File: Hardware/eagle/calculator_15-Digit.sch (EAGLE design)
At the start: 145 parts, among them M1 IRLML6402, M10 IRLML6402, M11 IRLML6402, M12 IRLML6402, M2 IRLML6402, M3 IRLML6402, M4 IRLML6402, M5 IRLML6402, M6 IRLML6402, M7 IRLML6402, M8 IRLML6402, M9 IRLML6402, U1 74HC4051_MUX, U2 TC1262-3.3VDB, U3 ATMEGA1284P-PU, U5 CON, X1 MICROMATCH-12, X3 MICROMATCH-12, Y2 12MHz

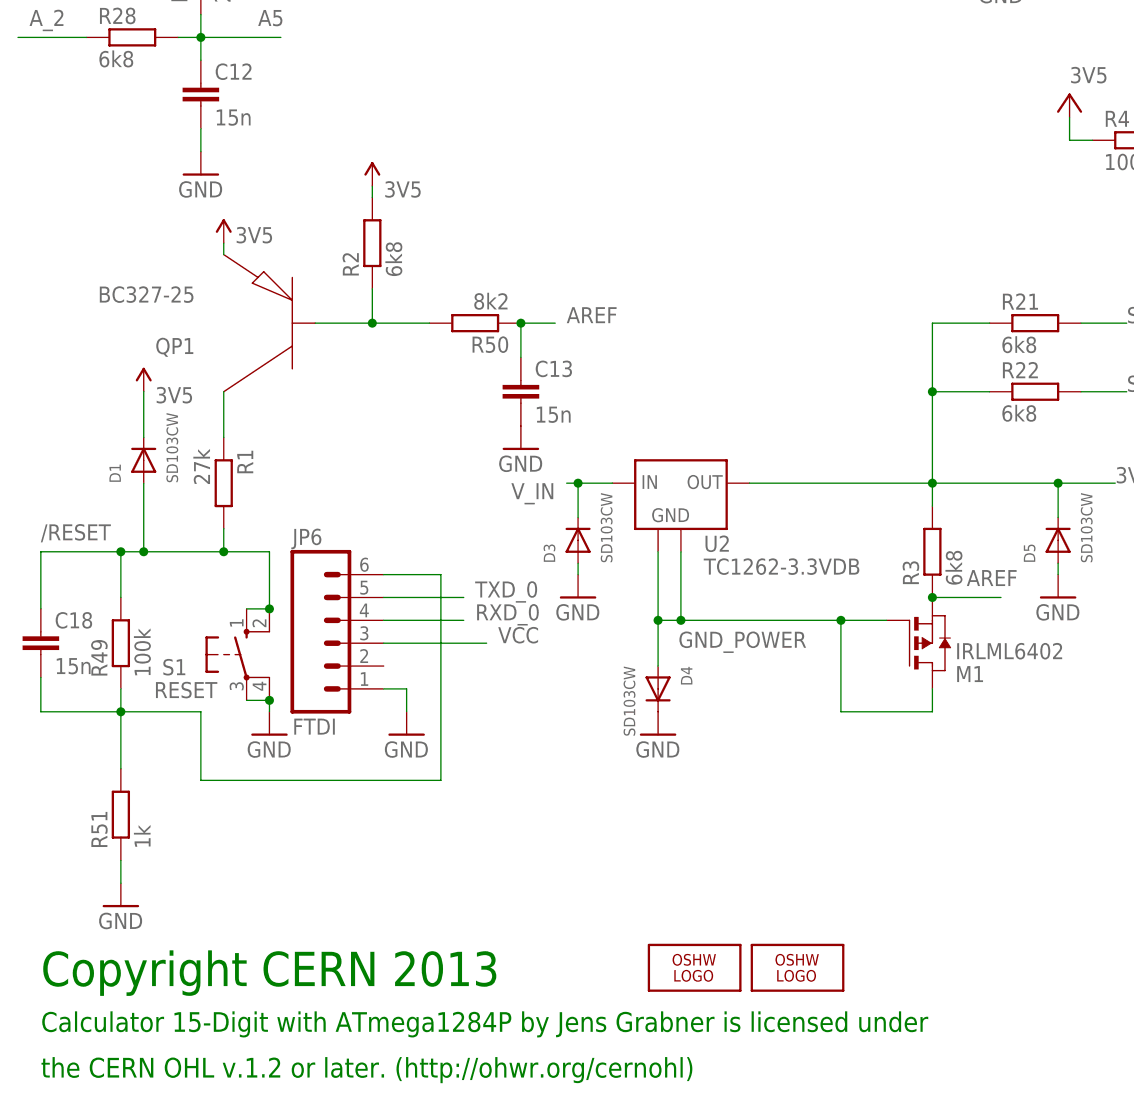
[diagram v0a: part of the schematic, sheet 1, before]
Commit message: new Switch Layout - with Kipptaster
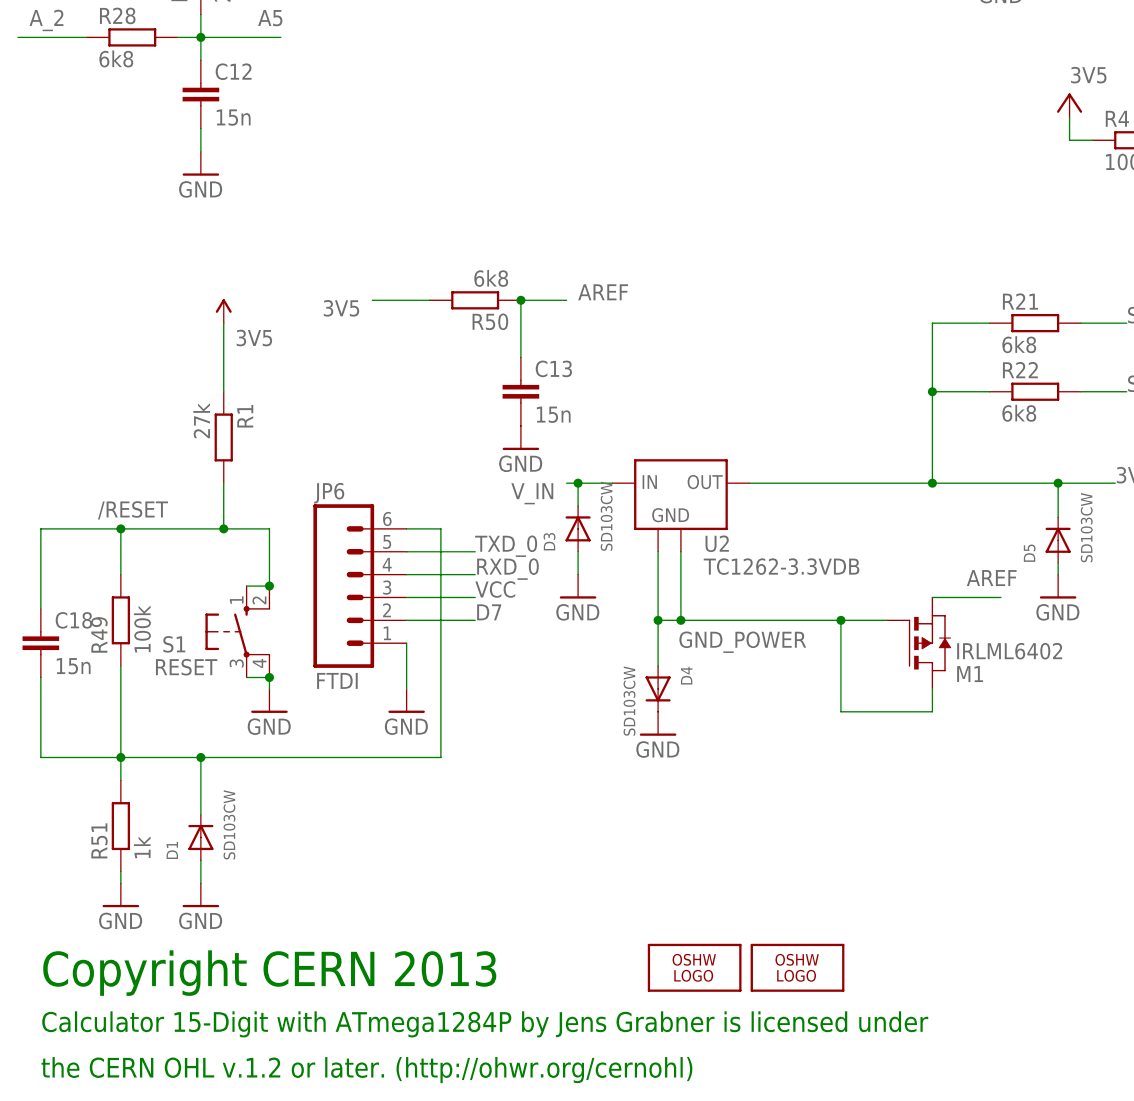
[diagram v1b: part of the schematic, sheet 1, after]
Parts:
- removed QP1: BC327-25, sym:PNP
- removed R2, R3: 6k8, rcl:R-EU_0204/7
- added JP13, JP14: PINHD-2X7, pinhead:PINHD-2X7
- R50: value 8k2 -> 6k8
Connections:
- removed net N$10: QP1.C, R1.1
- removed net N$13: QP1.B, R2.1, R50.2
- net /RESET: no longer D1.A
- net 3V5: now also R1.1; no longer D1.C, QP1.E, R2.2, R3.2
- net AREF: no longer R3.1
- net CA_PWM: now also JP13.1, JP13.2, JP14.13, JP14.14, JP14.8
- net D10: now also JP13.9
- net D11: now also JP13.10
- net D12: now also JP14.1
- net D13: now also JP14.2
- net D19: now also JP14.7
- net D20: now also JP14.6
- net D21: now also JP14.5
- net D22: now also JP14.4
- net D23: now also JP14.3
- net D5: now also JP13.8
- net D6: now also JP13.7
- net D7: now also JP6.2
- net GND: now also D1.A
- net IO_A: now also JP13.6
- net IO_A__: now also JP13.11
- net IO_B: now also JP13.5
- net IO_B__: now also JP13.12
- net IO_C: now also JP13.4
- net IO_C__: now also JP13.13
- net IO_D: now also JP13.3
- net IO_DP: now also JP14.9
- net IO_D__: now also JP13.14
- net IO_E: now also JP14.12
- net IO_F: now also JP14.11
- net IO_G: now also JP14.10
- net N$12: now also D1.C
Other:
- moved on the sheet: D1, D3, JP6, R1, R49, R50, R51, S1

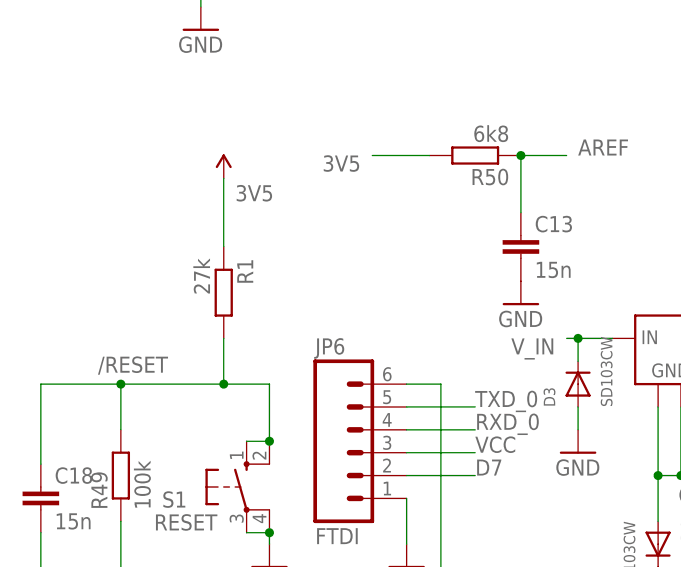
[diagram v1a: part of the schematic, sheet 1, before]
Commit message: MR(); MS(); M+=(); Display Status
Display whe to or more switch pressed.
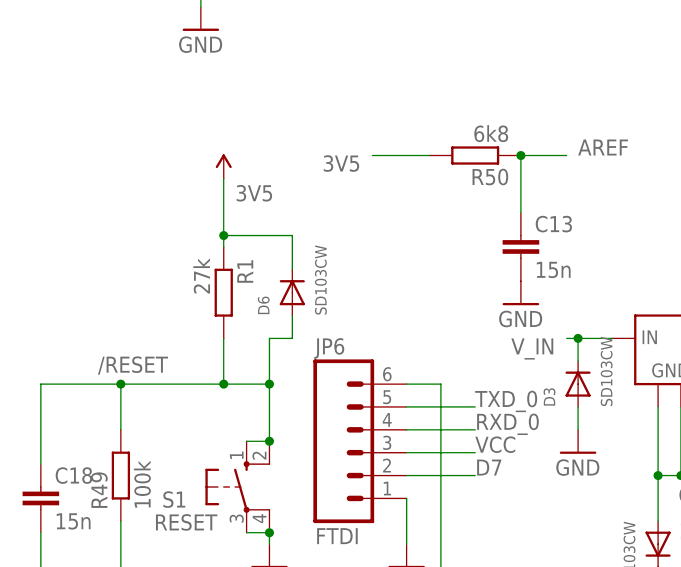
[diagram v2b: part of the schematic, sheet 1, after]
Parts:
- added D6: SD103CW, BaseApp:DIODESMA
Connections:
- net /RESET: now also D6.A
- net 3V5: now also D6.C
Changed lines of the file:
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@@
 <setting verticaltext="up"/>
 </settings>
-<grid distance="50" unitdist="mil" unit="mil" style="lines" multiple="1" display="no" altdistance="0.05" altunitdist="inch" altunit="inch"/>
+<grid distance="0.05" unitdist="inch" unit="inch" style="lines" multiple="1" display="no" altdistance="0.05" altunitdist="inch" altunit="inch"/>
 <layers>
 <layer number="1" name="Top" color="4" fill="1" visible="no" active="no"/>
@@
 <part name="D1" library="BaseApp" deviceset="DIODE" device="SMA" value="SD103CW"/>
 <part name="GND7" library="SparkFun" deviceset="GND" device=""/>
+<part name="D6" library="BaseApp" deviceset="DIODE" device="SMA" value="SD103CW"/>
 </parts>
 <sheets>
@@
 <attribute name="VALUE" x="20.32" y="21.59" size="1.778" layer="96"/>
 </instance>
+<instance part="D6" gate="G$1" x="33.02" y="76.2" rot="R90"/>
 </instances>
 <busses>
@@
 <pinref part="R1" gate="G$1" pin="2"/>
 <pinref part="R49" gate="G$1" pin="2"/>
+<wire x1="30.48" y1="66.04" x2="30.48" y2="71.12" width="0.1524" layer="91"/>
+<junction x="30.48" y="66.04"/>
+<wire x1="30.48" y1="71.12" x2="33.02" y2="71.12" width="0.1524" layer="91"/>
+<pinref part="D6" gate="G$1" pin="A"/>
+<wire x1="33.02" y1="71.12" x2="33.02" y2="73.66" width="0.1524" layer="91"/>
 </segment>
 <segment>
@@
 <pinref part="P+5" gate="1" pin="VCC"/>
 <label x="26.67" y="86.36" size="1.778" layer="95"/>
-<wire x1="25.4" y1="81.28" x2="25.4" y2="88.9" width="0.1524" layer="91"/>
+<wire x1="25.4" y1="81.28" x2="25.4" y2="82.55" width="0.1524" layer="91"/>
 <pinref part="R1" gate="G$1" pin="1"/>
-</segment>
-<segment>
+<pinref part="D6" gate="G$1" pin="C"/>
+<wire x1="25.4" y1="82.55" x2="25.4" y2="88.9" width="0.1524" layer="91"/>
+<wire x1="33.02" y1="78.74" x2="33.02" y2="82.55" width="0.1524" layer="91"/>
+<wire x1="33.02" y1="82.55" x2="25.4" y2="82.55" width="0.1524" layer="91"/>
+<junction x="25.4" y="82.55"/>
+</segment>
+<segment>

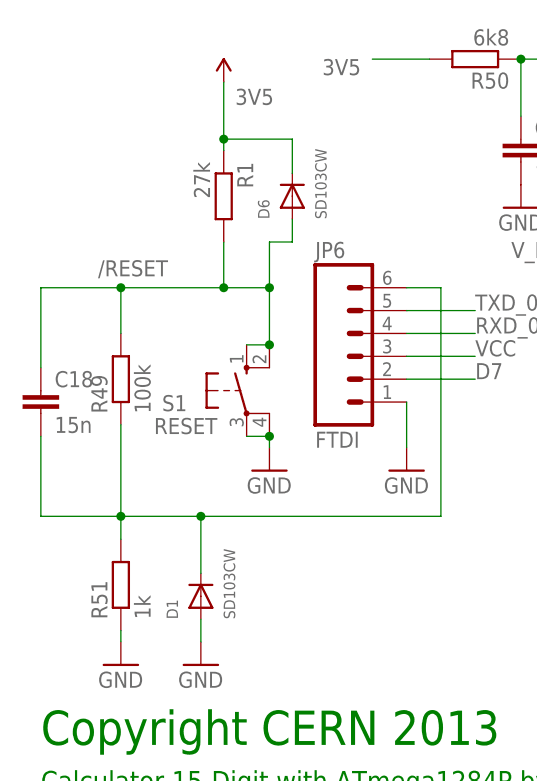
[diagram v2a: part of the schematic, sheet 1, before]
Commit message: RingBufCPP added
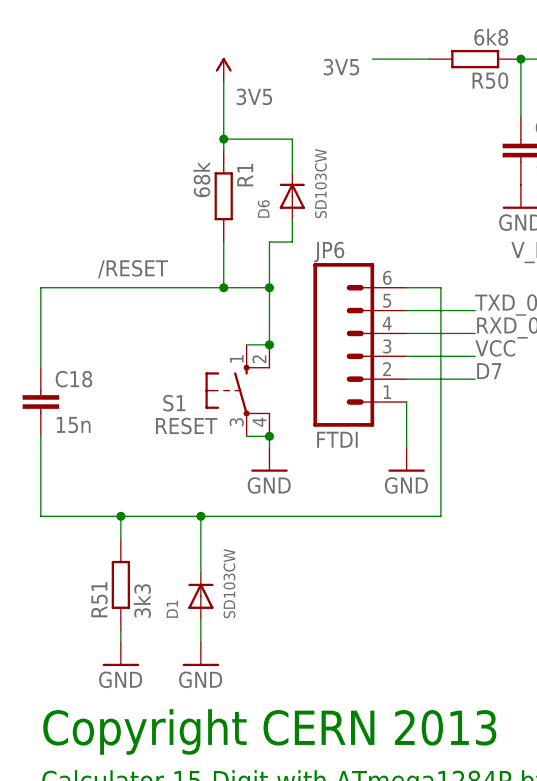
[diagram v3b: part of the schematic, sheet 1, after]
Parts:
- removed R49: 100k, rcl:R-EU_0204/7
- M10, M11, M3, M4, M5, M6, M7, M8, M9: value IRLML6402 -> IRLML6401
- R1: value 27k -> 68k
- R51: value 1k -> 3k3
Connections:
- net /RESET: no longer R49.2
- net N$12: no longer R49.1
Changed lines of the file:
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@@
 <setting verticaltext="up"/>
 </settings>
-<grid distance="0.05" unitdist="inch" unit="inch" style="lines" multiple="1" display="no" altdistance="0.05" altunitdist="inch" altunit="inch"/>
+<grid distance="0.1" unitdist="inch" unit="inch" style="lines" multiple="1" display="no" altdistance="0.05" altunitdist="inch" altunit="inch"/>
 <layers>
 <layer number="1" name="Top" color="4" fill="1" visible="no" active="no"/>
@@
 <part name="GND20" library="SparkFun" deviceset="GND" device=""/>
 <part name="GND21" library="SparkFun" deviceset="GND" device=""/>
-<part name="M3" library="IRLML6402" deviceset="IRLML6402" device=""/>
-<part name="M4" library="IRLML6402" deviceset="IRLML6402" device=""/>
-<part name="M5" library="IRLML6402" deviceset="IRLML6402" device=""/>
-<part name="M6" library="IRLML6402" deviceset="IRLML6402" device=""/>
-<part name="M7" library="IRLML6402" deviceset="IRLML6402" device=""/>
-<part name="M8" library="IRLML6402" deviceset="IRLML6402" device=""/>
-<part name="M9" library="IRLML6402" deviceset="IRLML6402" device=""/>
-<part name="M10" library="IRLML6402" deviceset="IRLML6402" device=""/>
-<part name="M11" library="IRLML6402" deviceset="IRLML6402" device=""/>
+<part name="M3" library="IRLML6402" deviceset="IRLML6402" device="" value="IRLML6401"/>
+<part name="M4" library="IRLML6402" deviceset="IRLML6402" device="" value="IRLML6401"/>
+<part name="M5" library="IRLML6402" deviceset="IRLML6402" device="" value="IRLML6401"/>
+<part name="M6" library="IRLML6402" deviceset="IRLML6402" device="" value="IRLML6401"/>
+<part name="M7" library="IRLML6402" deviceset="IRLML6402" device="" value="IRLML6401"/>
+<part name="M8" library="IRLML6402" deviceset="IRLML6402" device="" value="IRLML6401"/>
+<part name="M9" library="IRLML6402" deviceset="IRLML6402" device="" value="IRLML6401"/>
+<part name="M10" library="IRLML6402" deviceset="IRLML6402" device="" value="IRLML6401"/>
+<part name="M11" library="IRLML6402" deviceset="IRLML6402" device="" value="IRLML6401"/>
 <part name="FRAME3" library="frames" deviceset="LETTER_L" device="" value="frame"/>
 <part name="D29" library="BaseApp" deviceset="DIODE" device="SMA" value="SD103CW"/>
@@
 <part name="U3" library="Atmel_By_element14_Batch_1-00" deviceset="ATMEGA1284P-PU" device=""/>
 <part name="R50" library="rcl" deviceset="R-EU_" device="0204/7" value="6k8"/>
-<part name="R1" library="rcl" deviceset="R-EU_" device="0204/7" value="27k"/>
+<part name="R1" library="rcl" deviceset="R-EU_" device="0204/7" value="68k"/>
 <part name="R4" library="rcl" deviceset="R-EU_" device="0204/7" value="100"/>
-<part name="R49" library="rcl" deviceset="R-EU_" device="0204/7" value="100k"/>
-<part name="R51" library="rcl" deviceset="R-EU_" device="0204/7" value="1k"/>
+<part name="R51" library="rcl" deviceset="R-EU_" device="0204/7" value="3k3"/>
 <part name="R34" library="rcl" deviceset="R-EU_" device="0204/7" value="6k8"/>
 <part name="R48" library="rcl" deviceset="R-EU_" device="0204/7" value="1k"/>
@@
 <instance part="R1" gate="G$1" x="25.4" y="76.2" rot="R270"/>
 <instance part="R4" gate="G$1" x="127" y="109.22"/>
-<instance part="R49" gate="G$1" x="13.97" y="55.88" rot="R90"/>
 <instance part="R51" gate="G$1" x="13.97" y="33.02" rot="R90"/>
 <instance part="JP1" gate="G$1" x="238.76" y="113.03"/>
@@
 <segment>
 <wire x1="30.48" y1="66.04" x2="25.4" y2="66.04" width="0.1524" layer="91"/>
-<wire x1="25.4" y1="66.04" x2="13.97" y2="66.04" width="0.1524" layer="91"/>
-<wire x1="13.97" y1="66.04" x2="5.08" y2="66.04" width="0.1524" layer="91"/>
+<wire x1="25.4" y1="66.04" x2="5.08" y2="66.04" width="0.1524" layer="91"/>
 <wire x1="30.48" y1="66.04" x2="30.48" y2="59.69" width="0.1524" layer="91"/>
 <label x="11.43" y="67.31" size="1.778" layer="95"/>
@@
 <wire x1="25.4" y1="71.12" x2="25.4" y2="66.04" width="0.1524" layer="91"/>
 <junction x="25.4" y="66.04"/>
-<wire x1="13.97" y1="60.96" x2="13.97" y2="66.04" width="0.1524" layer="91"/>
-<junction x="13.97" y="66.04"/>
 <pinref part="C18" gate="G$1" pin="1"/>
 <pinref part="R1" gate="G$1" pin="2"/>
-<pinref part="R49" gate="G$1" pin="2"/>
 <wire x1="30.48" y1="66.04" x2="30.48" y2="71.12" width="0.1524" layer="91"/>
 <junction x="30.48" y="66.04"/>
@@
 <wire x1="13.97" y1="38.1" x2="13.97" y2="40.64" width="0.1524" layer="91"/>
 <pinref part="C18" gate="G$1" pin="2"/>
-<wire x1="13.97" y1="40.64" x2="13.97" y2="50.8" width="0.1524" layer="91"/>
 <wire x1="5.08" y1="49.53" x2="5.08" y2="40.64" width="0.1524" layer="91"/>
 <wire x1="5.08" y1="40.64" x2="13.97" y2="40.64" width="0.1524" layer="91"/>
@@
 <wire x1="49.53" y1="40.64" x2="22.86" y2="40.64" width="0.1524" layer="91"/>
 <wire x1="13.97" y1="40.64" x2="22.86" y2="40.64" width="0.1524" layer="91"/>
-<pinref part="R49" gate="G$1" pin="1"/>
 <pinref part="R51" gate="G$1" pin="2"/>
 <pinref part="D1" gate="G$1" pin="C"/>

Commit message: New Hardware Design V0.4
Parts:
- removed BH1, BH2, BH3: BATTERY_HOLDER_AAAHOLDER_AAA, SparkFun-Electromechanical:BATTERY_HOLDER_AAAHOLDER_AAA
- removed C12, C19: 15n, rcl:C-EU025_050-025X075
- removed C17: 1n, rcl:C-EU025_050-025X075
- removed C9: 2µ2, _jc:C-US025_050-025X075
- removed D29: SD103CW, BaseApp:DIODESMA
- removed JP3: DCF77, adafruit:PINHD-1X1CB
- removed M12, M2: IRLML6402, IRLML6402:IRLML6402
- removed R27, R45: 27k, rcl:R-EU_0204/7
- removed R28: 6k8, rcl:R-EU_0204/7
- removed R44: 47k, rcl:R-EU_0204/7
- removed R46, R47, R53: 8k2, rcl:R-EU_0204/7
- removed R52: 22, rcl:R-EU_0204/7
- removed S2: RESET, _jc:10-XX
- removed U2: TC1262-3.3VDB, parts:TC1262-3.3VDB
- removed U5: CON, BaseApp:AUDIO-JACKPTH
- added BH10, BH12, BH8: HOLDER_AAA_RIGHT, SparkFun-Electromechanical:HOLDER_AAA_RIGHT
- added BH11, BH7, BH9: HOLDER_AAA_LEFT1, SparkFun-Electromechanical:HOLDER_AAA_LEFT1
- added C16: 0.1uF, SparkFun:CAP0805
- added C20, C21: 10uF, SparkFun:CAP_POL1206
- added C22: 15n, rcl:C-EUC1206K
- added D10, D7, D8, D9: SD103CW, BaseApp:DIODESMA
- added R2: 6k8, rcl:R-EU_0204/5
- added R3: 27k, rcl:R-EU_R1206
- added S3: B3F-4150, SmartPrj:TACTILE_SWITCHTACTILE_SWITCH_PTH-12MM
- added U$1: IRLML6244, transistor-power:IRLML2502
- added U4: TLV70033, SparkFun:V_REG_LDOSMD
- C10: device rcl:C-EU025_050-025X075 -> rcl:C-EUC1206K
- C11: value 15n -> 1n; device rcl:C-EU025_050-025X075 -> SparkFun:CAP0805
- C5: value 2µ2 -> 15n; device _jc:C-US025_050-025X075 -> rcl:C-EUC1206K
- JP13, JP14: value PINHD-2X7 -> (none)
- M1: value IRLML6402 -> IRLML2244
- M10, M11, M3, M4, M5, M6, M7, M8, M9: value IRLML6401 -> IRLML2244
- R20: value 27k -> 2R7; device rcl:R-EU_0204/7 -> rcl:R-EU_0204/5
- R23: value 27k -> 6k8; device rcl:R-EU_0204/7 -> rcl:R-EU_R1206
- R24: value 6k8 -> 2R7; device rcl:R-EU_0204/7 -> rcl:R-EU_R1206
- R25: value 27k -> 100
- R26: value 6k8 -> 27k; device rcl:R-EU_0204/7 -> rcl:R-EU_0204/5
- R30: value 3k3 -> 3V3
- R31: value 68 -> 39
- R32: value 100 -> 39
- R35: value 8k2 -> 3k3
- R48: value 1k -> 3k3
- SG1: value BUZZERPTH-KIT -> BUZZERNS; device SparkFun-Electromechanical:BUZZERPTH-KIT -> SparkFun-Electromechanical:BUZZERNS
- U$2: value IRLML2502 -> IRLML6244
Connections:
- net D11 renamed D5_
- net D12 renamed D6_
- net D13 renamed D7_
- net D14 renamed D0_
- net RXD_0 renamed D8_
- net TXD_0 renamed D9_
- removed net 3V5: C1.1, C2.1, C3.1, C6.1, D5.C, D6.C, JP5.VCC, R1.1, R21.1, R22.1, R4.1, U2.OUT, U3.VCC
- removed net A_0: KP1.C2, KP2.C2, R24.1
- removed net A_1: KP1.C1, KP2.C1, R26.1
- removed net A_2: KP1.C0, KP2.C0, R28.1
- removed net D4: C17.1, R35.1, U3.PD4
- removed net INH: R45.1, U$2.D, U1.INH
- removed net N$24: C15.1, R31.1, R32.2
- removed net N$29: M3.G, R34.1, R48.2
- removed net N$8: C19.1, M12.G, M2.G, R45.2, R47.1
- removed net N$9: R46.1, R47.2, S2.S, S2.S1
- removed net OFF: D29.A, R20.2, R44.1, U$2.G
- removed net SEG_C_SOURCE: JP10.1, M6.D
- removed net SEG_DP_SOURCE: JP7.1, M11.D
- removed net V_DCF77: C9.1, R52.2, R53.1, U5.LEFT
- new net 3V3: C1.1, C16.1, C2.1, C20.+, C3.1, C6.1, D5.C, D6.C, D7.A, R1.1, R21.1, R22.1, R4.1, U3.VCC, U4.OUT
- new net A8: C22.1, R35.1, R48.2
- new net A9: C5.1, R25.1, R26.2, R3.2
- new net D12_: D9.A, D9.C, R48.1, U$1.D, U$1.S, U3.PD4
- new net EN: C10.1, C5.2, D10.C, R2.2, R23.2, R26.1, R3.1, U$2.G, U4.EN
- new net GND1: C22.2
- new net IO: U$2.D, U1.IO
- new net N$6: S3.3, S3.4
- new net XX4: C14.2, C15.2, R32.1, SG1.2
- new net XX_3: D8.A, R20.1, R24.1
- net A0: now also C15.1, R31.1; no longer R32.1
- net A4: now also R32.2
- net A5: now also KP1.C0, KP2.C0; no longer C12.1, R27.1, R28.2
- net A6: now also KP1.C1, KP2.C1; no longer C11.1, R25.1, R26.2
- net A7: now also KP1.C2, KP2.C2; no longer C10.1, R23.1, R24.2
- net AREF: no longer C5.1, R23.2, R25.2, R27.2
- net D18: now also D10.A, U$1.G; no longer D29.C
- net D7: no longer JP3.1, JP6.2, R53.2, U5.RIGHT
- net GND: now also C16.2, C20.-, C21.-, JP6.2, R2.1, R23.1, S3.5, U1.INH, U4.GND; no longer BH1.-, C12.2, C14.2, C15.2, C5.2, C9.2, SG1.2, U1.IO, U5.SLEEVE
- net GND_POWER: no longer R20.1, S2.P, S2.P1, U$2.S, U2.GND, U2.GND1
- net N$1: now also M3.G, R34.1; no longer C17.2, R48.1
- net N$2: now also U$2.S; no longer BH1.+, BH2.-
- net N$3: now also C11.1, U4.BP; no longer BH2.+, BH3.-
- net N$7: now also D8.C; no longer M12.S, M2.S, R46.2
- net NC1: now also BH11.+, BH7.+, BH9.+
- net NC3: now also BH10.-, BH12.-, BH8.-
- net SEG_C: now also JP10.1, M6.D
- net SEG_DP: now also JP7.1, M11.D
- net VCC: now also JP5.VCC, R20.2, R24.2; no longer BH3.+, M2.D
- net V_IN: now also C21.+, D7.C, S3.1, S3.2, U4.IN; no longer C19.2, M12.D, R44.2, R52.1, U2.IN
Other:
- note added: "Board is marked with combination of"
- note added: "Max Current Output: 100mA"
- note added: "Max Voltage Input: 10VDC"
- note added: "VCC = 3.3V Output"
- note added: "resonator frequency and regulator voltage."
- moved on the sheet: C10, C11, C14, C15, D3, D4, M1, R23, R24, R25, R26, R31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
